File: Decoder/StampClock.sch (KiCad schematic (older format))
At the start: 7 parts, among them J981 USB_B, SW981 BOOTSEL, SW982 RUN STOP, SW983 +/T, SW984 -/S, U981 RP2040_Stamp, U982 74LVC245

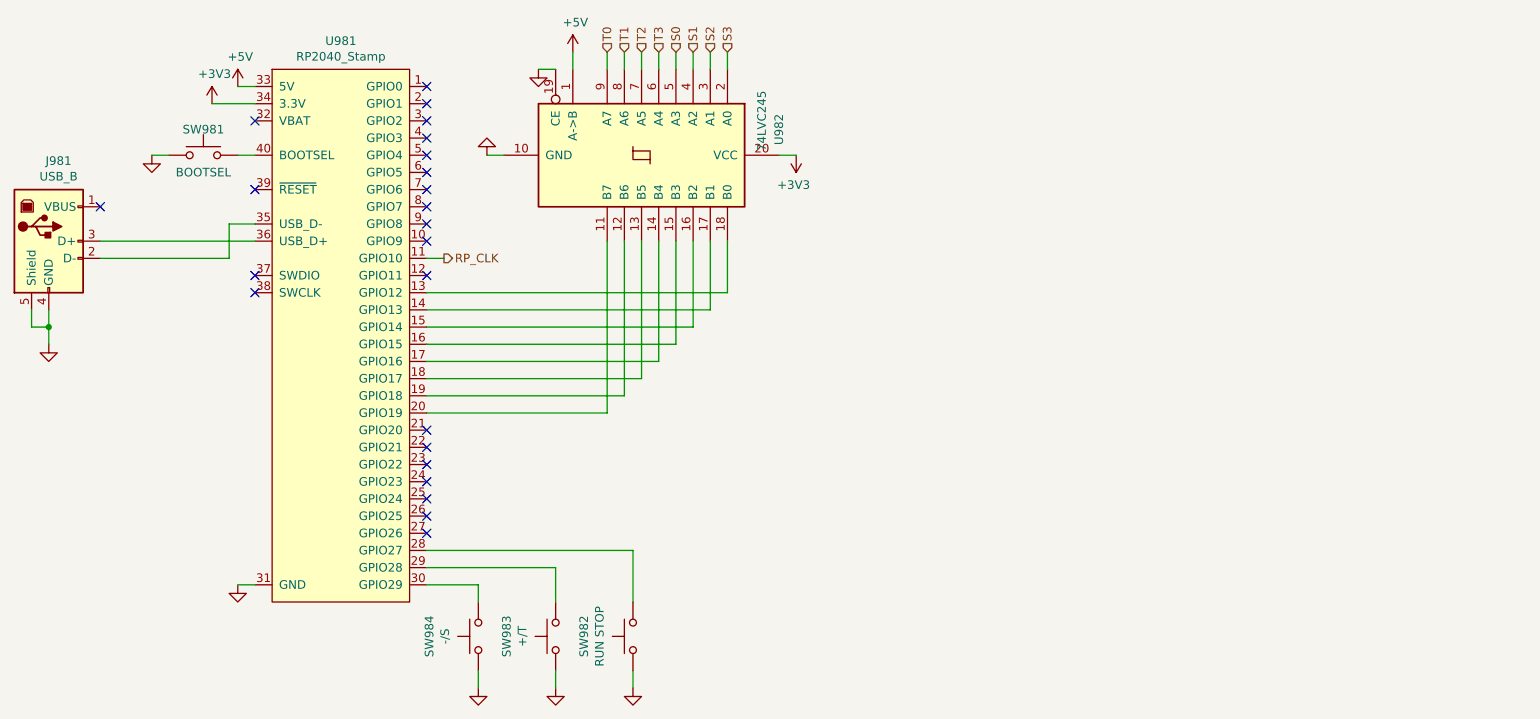
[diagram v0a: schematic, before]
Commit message: Schematics for display & keyboard, adding LEDs to processor PCB
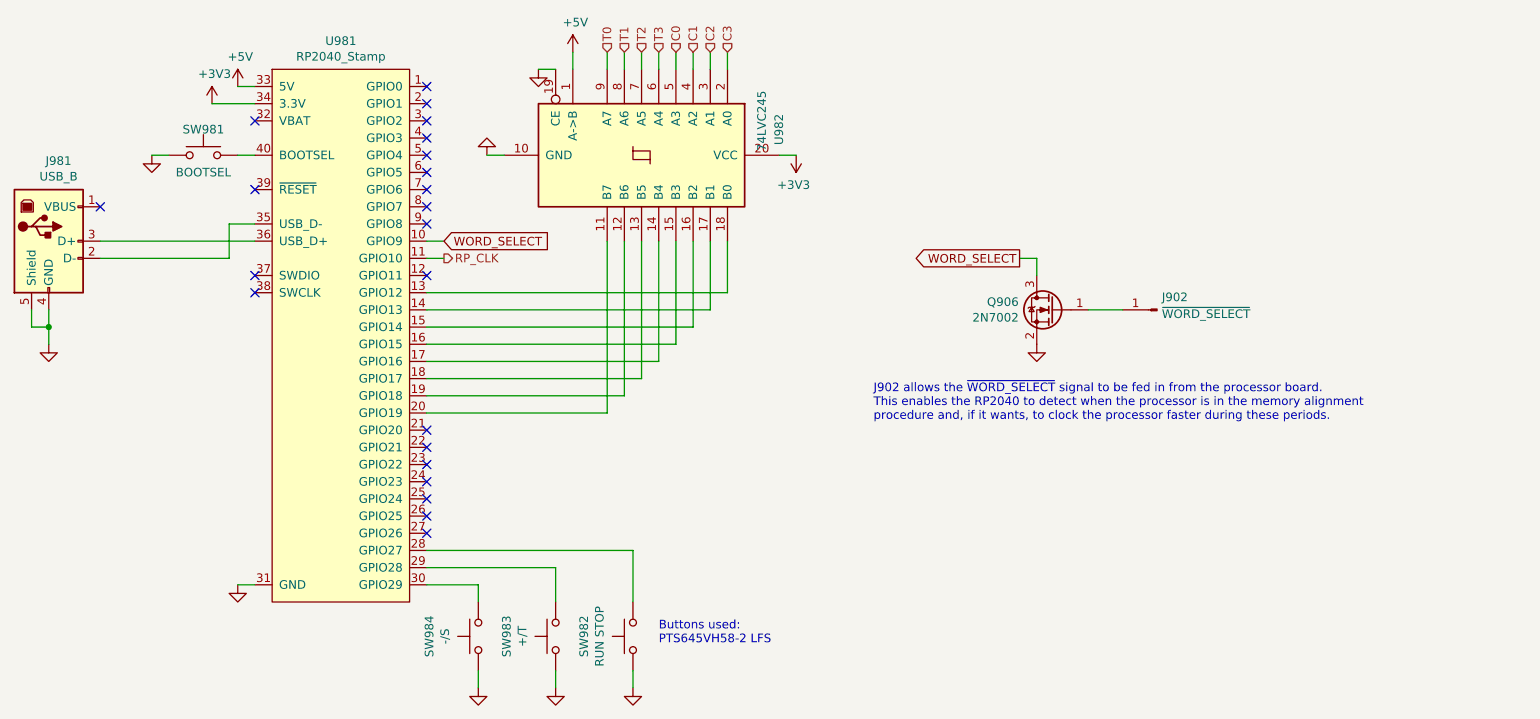
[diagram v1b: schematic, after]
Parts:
- added J902: ~WORD_SELECT, Connector_PinHeader_2.54mm:PinHeader_1x01_P2.54mm_Horizontal, symbol Connector:Conn_01x01_Male
- added Q906: 2N7002, Package_TO_SOT_SMD:SOT-23, symbol Transistor_FET:2N7002
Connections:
- net GND: now also Q906.2 (S)
- net WORD_SELECT: now reaches U981.10 (GPIO9)
- net WORD_SELECT: now also Q906.3 (D)
- net S0 renamed C0
- net S1 renamed C1
- net S2 renamed C2
- net S3 renamed C3
- new net: J902.1 (Pin_1), Q906.1 (G)
- no-connect marks 23 -> 22
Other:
- note added: "Buttons used:\nPTS645VH58-2 LFS"
- note added: "J902 allows the ~WORD_SELECT~ signal to be fed in from the processor board.\nThis enables the RP2040 to detect when the processor is in the memory alignment\nprocedure and, if it wants, to clock the processor faster during these periods."
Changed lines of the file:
@@
 $EndComp
 Text HLabel 4650 1850 1    50   Input ~ 0
-S0
+C0
 Text HLabel 4750 1850 1    50   Input ~ 0
-S1
+C1
 Text HLabel 4850 1850 1    50   Input ~ 0
-S2
+C2
 Text HLabel 4950 1850 1    50   Input ~ 0
-S3
+C3
 Text HLabel 4250 1850 1    50   Input ~ 0
 T0
@@
 NoConn ~ 3200 2750
 NoConn ~ 3200 2850
-NoConn ~ 3200 2950
 NoConn ~ 3200 3150
-NoConn ~ 3200 4050
 NoConn ~ 3200 4150
 NoConn ~ 3200 4250
@@
 	1    0    0    -1
 $EndComp
+$Comp
+L Transistor_FET:2N7002 Q906
+U 1 1 64B6B74A
+P 6850 3350
+F 0 "Q906" H 7055 3396 50  0000 L CNN
+F 1 "2N7002" H 7055 3305 50  0000 L CNN
+F 2 "Package_TO_SOT_SMD:SOT-23" H 7050 3275 50  0001 L CIN
+F 3 "https://www.onsemi.com/pub/Collateral/NDS7002A-D.PDF" H 6850 3350 50  0001 L CNN
+	1    6850 3350
+	-1   0    0    -1
+$EndComp
+$Comp
+L power:GND #PWR0904
+U 1 1 64B7371B
+P 6750 3550
+F 0 "#PWR0904" H 6750 3300 50  0001 C CNN
+F 1 "GND" H 6755 3377 50  0001 C CNN
+F 2 "" H 6750 3550 50  0001 C CNN
+F 3 "" H 6750 3550 50  0001 C CNN
+	1    6750 3550
+	1    0    0    -1
+$EndComp
+$Comp
+L Connector:Conn_01x01_Male J902
+U 1 1 64B752BB
+P 7450 3350
+F 0 "J902" H 7422 3276 50  0000 R CNN
+F 1 "~WORD_SELECT" H 7422 3374 50  0000 R CNN
+F 2 "Connector_PinHeader_2.54mm:PinHeader_1x01_P2.54mm_Horizontal" H 7450 3350 50  0001 C CNN
+F 3 "~" H 7450 3350 50  0001 C CNN
+	1    7450 3350
+	-1   0    0    1
+$EndComp
+Wire Wire Line
+	7250 3350 7050 3350
+Wire Wire Line
+	6750 3050 6750 3150
+Text Notes 5800 4000 0    50   ~ 0
+J902 allows the ~WORD_SELECT~ signal to be fed in from the processor board.\nThis enables the RP2040 to detect when the processor is in the memory alignment\nprocedure and, if it wants, to clock the processor faster during these periods.
+Text GLabel 3300 2950 2    50   Input ~ 0
+WORD_SELECT
+Wire Wire Line
+	3300 2950 3200 2950
+Text GLabel 6650 3050 0    50   Output ~ 0
+WORD_SELECT
+Wire Wire Line
+	6650 3050 6750 3050
+NoConn ~ 3200 4050
+Text Notes 4550 5300 0    50   ~ 0
+Buttons used:\nPTS645VH58-2 LFS
 $EndSCHEMATC
